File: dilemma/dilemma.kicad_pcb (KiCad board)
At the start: 2 copper layers, 142.3 x 95.1 mm, 79 parts, among them J1 S3B-PH-SM4-TB(LF)(SN), J2 Serial, J3 BATTERY_CONN_DEANS, J5 S3B-PH-SM4-TB(LF)(SN), SW1 SW_Push, SW10 SW_Push, SW11 SW_Push, SW12 SW_Push, SW13 SW_Push, SW14 SW_Push, SW15 SW_Push, SW16 SW_Push, SW17 SW_Push, SW2 SW_Push, SW26 SW_SPST, SW3 SW_Push, SW37 SW_SPST, SW4 SW_Push, SW5 SW_Push, SW6 SW_Push, SW7 SW_Push, SW8 SW_Push, SW9 SW_Push, U2 eliteC

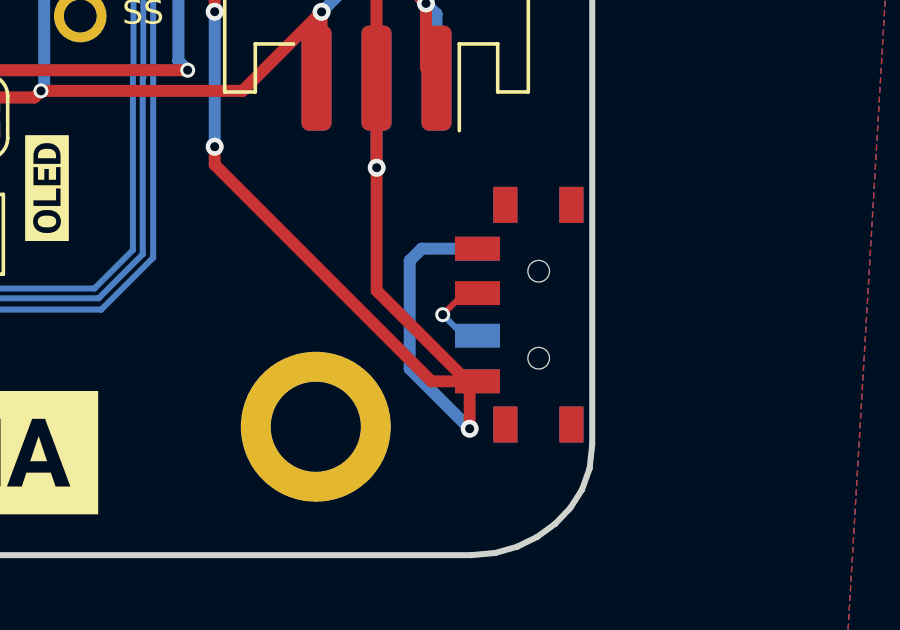
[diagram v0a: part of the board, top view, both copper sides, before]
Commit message: connect power switch pads
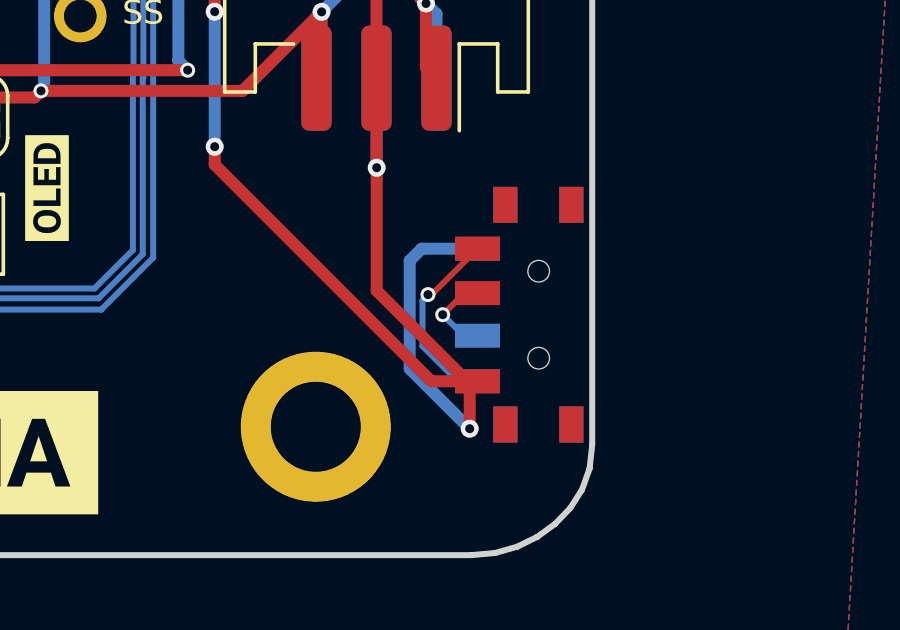
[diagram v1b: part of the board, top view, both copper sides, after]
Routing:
- net unconnected-(PSW1-Pad3): track 0.00 -> 6.40 mm, vias 0 -> 1
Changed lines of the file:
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@@
   (segment (start 224.784861 69.117008) (end 224.943332 68.958537) (width 0.2) (layer "B.Cu") (net 42))
   (segment (start 224.784861 72.22) (end 224.784861 69.117008) (width 0.2) (layer "B.Cu") (net 42))
+  (segment (start 242.93 74.23) (end 242.81 74.23) (width 0.2) (layer "F.Cu") (net 43))
+  (segment (start 244.46 72.7) (end 242.93 74.23) (width 0.2) (layer "F.Cu") (net 43))
+  (via (at 242.81 74.23) (size 0.5) (drill 0.3) (layers "F.Cu" "B.Cu") (net 43))
+  (segment (start 242.81 74.23) (end 242.62752 74.41248) (width 0.2) (layer "B.Cu") (net 43))
+  (segment (start 242.62752 74.41248) (end 242.62752 75.95) (width 0.2) (layer "B.Cu") (net 43))
+  (segment (start 243.79752 77.12) (end 244.46 77.12) (width 0.2) (layer "B.Cu") (net 43))
+  (segment (start 242.62752 75.95) (end 243.79752 77.12) (width 0.2) (layer "B.Cu") (net 43))
   (zone (net 23) (net_name "Gnd_l") (layers F&B.Cu) (hatch edge 0.508)
     (connect_pads (clearance 0.508))

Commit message: silkscreen
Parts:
- added kibuzzard-61F01A92: G***, kibuzzard-61F01A92, F.Cu at (204.5, 58.4)
- added kibuzzard-61F01A92: G***, kibuzzard-61F01A92, B.Cu at (204.5, 58.3)
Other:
- board text added: "BastardKB x Freznel"

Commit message: Footprint cleanup
Added power switch footprint to local lib
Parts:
- PSW1: footprint used_footprints:Switch_MSK-12C01-07 -> local-libraries:Switch_MSK-12C01-07

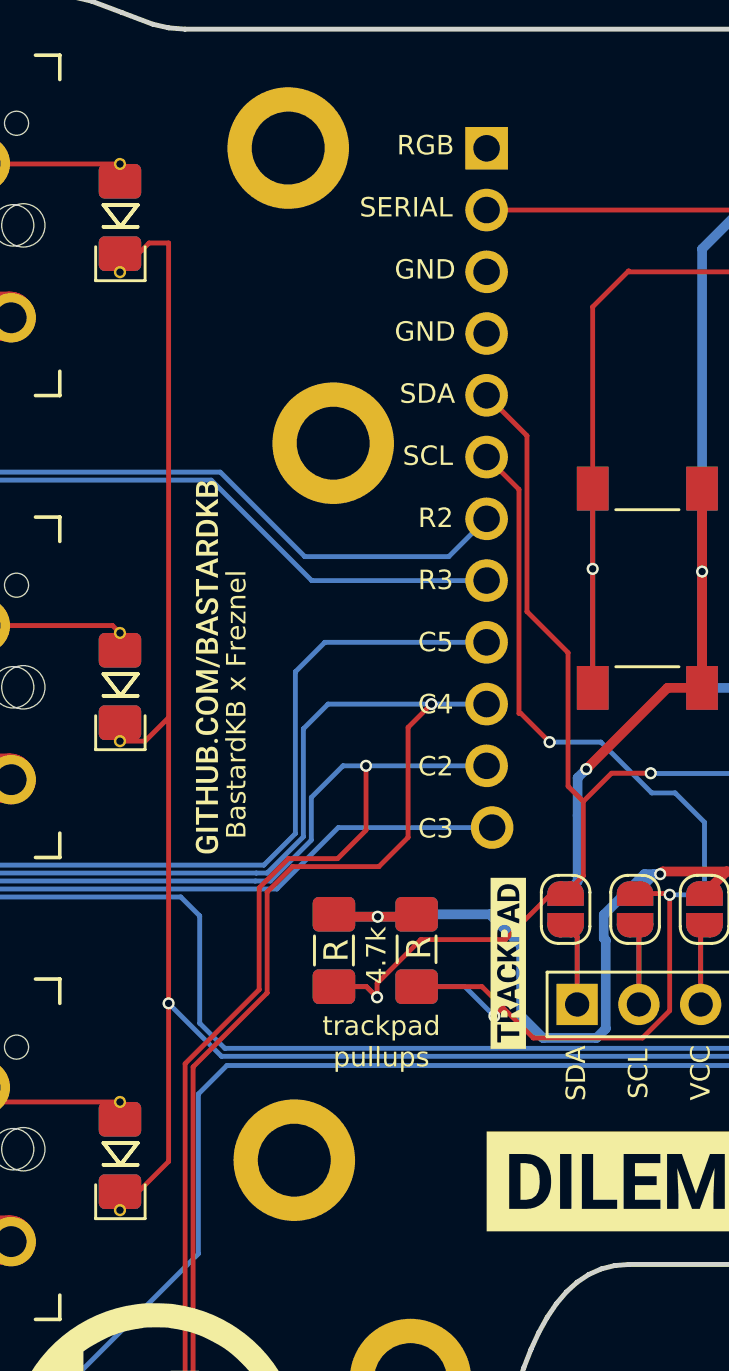
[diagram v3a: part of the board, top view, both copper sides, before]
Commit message: Schematic reference update
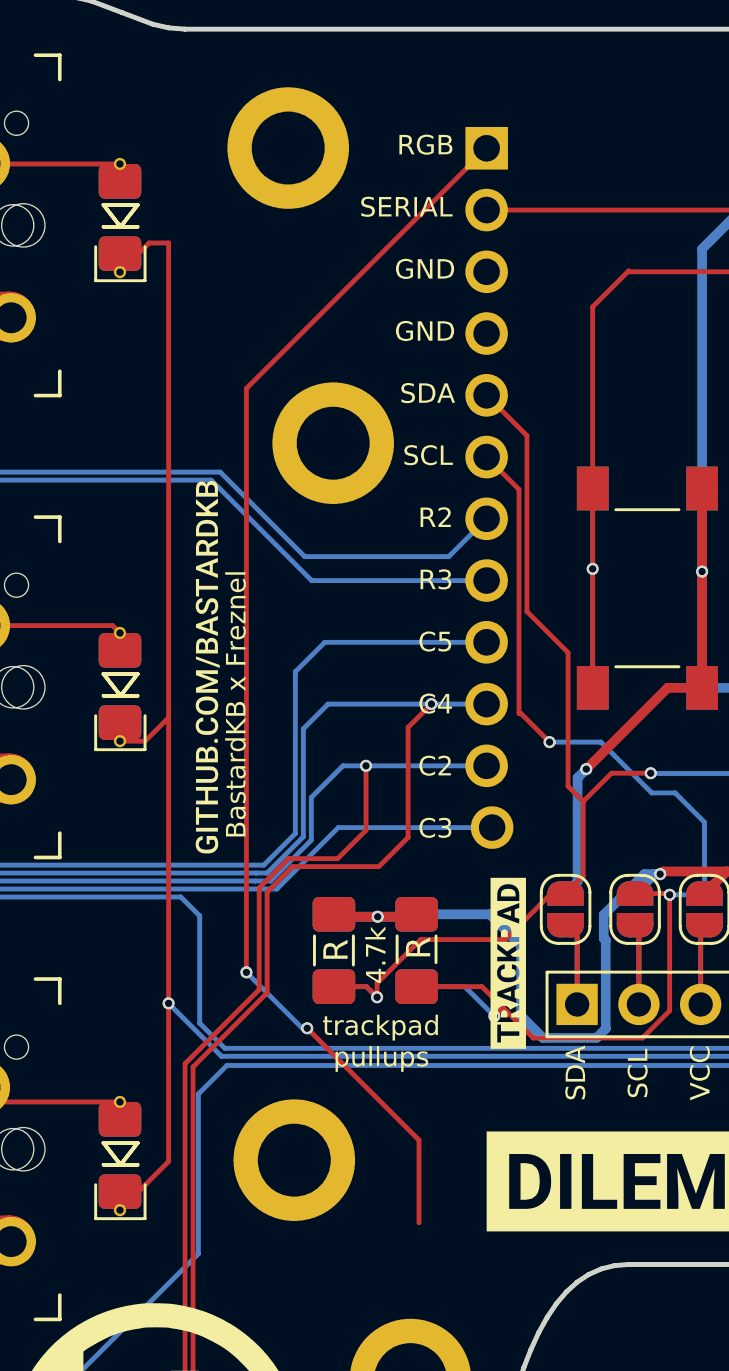
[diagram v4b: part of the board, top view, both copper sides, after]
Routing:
- net rgb_l: track 0.00 -> 51.3 mm, vias 0 -> 2
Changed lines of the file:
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@@
   (segment (start 242.2 76.7) (end 244.2 78.7) (width 0.4) (layer "B.Cu") (net 29))
   (segment (start 244.46 72.7) (end 242.6 72.7) (width 0.4) (layer "B.Cu") (net 29))
+  (segment (start 213.2 77.8) (end 213.2 81.2) (width 0.2) (layer "F.Cu") (net 30))
+  (segment (start 215.98 37.005) (end 206.1 46.885) (width 0.2) (layer "F.Cu") (net 30))
+  (segment (start 206.1 46.885) (end 206.1 70.9) (width 0.2) (layer "F.Cu") (net 30))
+  (segment (start 208.6 73.2) (end 213.2 77.8) (width 0.2) (layer "F.Cu") (net 30))
+  (via (at 208.6 73.2) (size 0.5) (drill 0.3) (layers "F.Cu" "B.Cu") (net 30))
+  (via (at 206.1 70.9) (size 0.5) (drill 0.3) (layers "F.Cu" "B.Cu") (net 30))
+  (segment (start 206.1 70.9) (end 208.4 73.2) (width 0.2) (layer "B.Cu") (net 30))
+  (segment (start 208.4 73.2) (end 208.6 73.2) (width 0.2) (layer "B.Cu") (net 30))
   (segment (start 231.76 33.14) (end 228.4 36.5) (width 0.2) (layer "F.Cu") (net 31))
   (segment (start 228.4 37.9) (end 226.755 39.545) (width 0.2) (layer "F.Cu") (net 31))

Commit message: chopped up
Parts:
- added JP9: JUMPER-SMT_3_NO, local-libraries:SolderJumper-3_P1.3mm_Open_RoundedPad1.0x1.5mm_NumberLabels, F.Cu at (238.3, 44.8)
- D10, D13, D14, D15, D18, D19, D20, D24, D25, D26, D3, D30, D33, D4, D5, D8, D9: footprint footprints:D_1206_handsolder_reversible -> local-libraries:D_1206_handsolder_reversible
- G*** (x4): footprint LOGO -> local-libraries:LOGO
- H1, H2, H3, H4, H5, H6, H7, H8, H9: footprint footprints:MountingHole_3mm_Pad_thin -> local-libraries:MountingHole_3mm_Pad_thin
- J1, J5: footprint Connector_JST:JST_PH_S3B-PH-SM4-TB_1x03-1MP_P2.00mm_Horizontal -> local-libraries:JST_SH_BM02B-SRSS-TB_1x02-1MP_P1.00mm_Vertical
- J2: footprint footprints:Jack_3.5mm_PJ320E_Horizontal_reversible -> local-libraries:Jack_3.5mm_PJ320E_Horizontal_reversible
- JP1, JP2, JP3, JP4, JP5, JP6, JP7, JP8: footprint footprints:SolderJumper-2_P1.3mm_Open_RoundedPad1.0x1.5mm -> local-libraries:SolderJumper-2_P1.3mm_Open_RoundedPad1.0x1.5mm
- O2: footprint footprints:PinHeader_1x04_P2.54mm_Vertical -> local-libraries:PinHeader_1x04_P2.54mm_Vertical
- R3, R4, R7: footprint footprints:R_1206_handsolder_reversible -> local-libraries:R_1206_handsolder_reversible
- SW1, SW10, SW11, SW12, SW13, SW14, SW15, SW16, SW2, SW3, SW4, SW5, SW6, SW7, SW8, SW9: footprint footprints:SW_MX_choc -> local-libraries:SW_MX_choc
- SW17: value SW_Push -> locked; footprint footprints:SW_MX_choc -> local-libraries:SW_MX_choc
- SW26, SW37: footprint footprints:SW_Push_1P1T_NO_6x6mm_H9.5mm -> local-libraries:SW_Push_1P1T_NO_6x6mm_H9.5mm
- kibuzzard-61F01A92 (x2): footprint kibuzzard-61F01A92 -> local-libraries:kibuzzard-61F01A92
- kibuzzard-61F01C84 (x2): footprint kibuzzard-61F01C84 -> local-libraries:kibuzzard-61F01C84
- kibuzzard-628D396A: footprint kibuzzard-628D396A -> local-libraries:kibuzzard-628D396A
- kibuzzard-628D3AA1: footprint kibuzzard-628D3AA1 -> local-libraries:kibuzzard-628D3AA1
- kibuzzard-628DFB48 (x2): footprint kibuzzard-628DFB48 -> local-libraries:kibuzzard-628DFB48
- kibuzzard-628DFB5F (x2): footprint kibuzzard-628DFB5F -> local-libraries:kibuzzard-628DFB5F
- kibuzzard-628DFB95 (x2): footprint kibuzzard-628DFB95 -> local-libraries:kibuzzard-628DFB95
- kibuzzard-628E0199 (x2): footprint kibuzzard-628E0199 -> local-libraries:kibuzzard-628E0199
- moved kibuzzard-61F01A92 64.0 mm to (268.5, 58.6)
- moved kibuzzard-628DFB95 60.5 mm to (271.7, 42.4) (x2)
- moved H3 60.4 mm to (268.1, 32.6)
- moved J2 36.8 mm to (231.3, 76.2), turned to -90 degrees
- moved PSW1 24.7 mm to (222.6, 81.3), turned to 0 degrees
- moved D25 17.4 mm to (186.8, 69.3), turned to 180 degrees
- moved D26 16.8 mm to (186.5, 87.0), turned to 180 degrees
- moved D24 16.7 mm to (186.9, 48.9), turned to 180 degrees
- moved H9 13.4 mm to (206.5, 36.1)
- moved H6 13.4 mm to (234.5, 36.1)
- moved H8 10.9 mm to (236.1, 68.1)
- moved H7 10.9 mm to (205.1, 68.1)
- moved R7 8.76 mm to (235.8, 44.6)
- moved R3 7.20 mm to (207.9, 77.0)
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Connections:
- J1 pad 1: Gnd_l -> bat_l
- J1 pad 2: bat_l -> Gnd_l
- J5 pad 1: Gnd_l -> bat_l
- J5 pad 2: bat_l -> Gnd_l
- R7 pad 1: Gnd_l -> hand
- R7 pad 2: Vcc_l -> Net-(R7-Pad2)
- U2 pad 20: Gnd_l -> hand
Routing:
- net Gnd_l: track 124.3 -> 7.91 mm, vias 7 -> 0
- net col5_l: track 99.6 -> 0.00 mm, vias 1 -> 0
- net bat_l: track 93.0 -> 7.86 mm, vias 4 -> 0
- net row1_l: track 129.6 -> 53.6 mm
- net Vcc_l: track 90.1 -> 19.7 mm, vias 4 -> 1
- net rgb_l: track 51.3 -> 0.00 mm, vias 2 -> 0
- net sda_l: track 48.5 -> 0.00 mm, vias 2 -> 0
- net scl_l: track 47.1 -> 0.00 mm, vias 3 -> 1
- net col3_l: track 160.6 -> 116.3 mm, vias 2 -> 1
- net row4_l: track 233.9 -> 190.0 mm
- net col1_l: track 179.2 -> 141.3 mm, vias 2 -> 1
- net Rst_l: track 35.5 -> 0.00 mm, vias 1 -> 0
- net serial_l: track 30.8 -> 0.00 mm
- net row3_l: track 211.0 -> 185.4 mm
- net row2_l: track 195.6 -> 173.1 mm
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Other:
- board size 142.3 x 95.1 mm -> 134 x 95.1 mm
